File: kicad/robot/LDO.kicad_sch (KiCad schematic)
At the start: 20 parts, among them U14 MAX77642ANA+

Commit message: Exported all schematic symbols to local robot and refer to them in all symbols
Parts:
- C4, C84, C85, C87, C88, C92, C93: symbol Device:C -> robot:C
- JP22: symbol Jumper:Jumper -> robot:Jumper
- JP7: symbol Jumper:Jumper_2_Bridged -> robot:Jumper_2_Bridged
- L3: symbol Device:L -> robot:L
- R53, R55, R9: symbol Device:R -> robot:R
- U14: symbol Regulator_Switching:MAX77642ANA+ -> robot:MAX77642ANA+
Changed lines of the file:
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@@
     (effects (font (size 1.27 1.27)) (justify right))
   )
-  (symbol (lib_id "Device:R") (at 26.67 106.68 0) (unit 1)
+  (symbol (lib_id "robot:R") (at 26.67 106.68 0) (unit 1)
     (in_bom yes) (on_board yes) (dnp no)
     (property "Reference" "R53" (at 29.21 105.4099 0)
@@
     )
   )
-  (symbol (lib_id "Device:C") (at 196.85 86.36 0) (mirror y) (unit 1)
+  (symbol (lib_id "robot:C") (at 196.85 86.36 0) (mirror y) (unit 1)
     (in_bom yes) (on_board yes) (dnp no)
     (property "Reference" "C93" (at 193.04 83.8199 0)
@@
     )
   )
-  (symbol (lib_id "Device:C") (at 151.13 88.9 0) (mirror y) (unit 1)
+  (symbol (lib_id "robot:C") (at 151.13 88.9 0) (mirror y) (unit 1)
     (in_bom yes) (on_board yes) (dnp no)
     (property "Reference" "C88" (at 147.32 86.3599 0)
@@
     )
   )
-  (symbol (lib_id "Jumper:Jumper_2_Bridged") (at 213.36 77.47 0) (unit 1)
+  (symbol (lib_id "robot:Jumper_2_Bridged") (at 213.36 77.47 0) (unit 1)
     (in_bom yes) (on_board yes) (dnp no)
     (property "Reference" "JP7" (at 213.36 74.93 0)
@@
     )
   )
-  (symbol (lib_id "Device:R") (at 46.99 106.68 0) (unit 1)
+  (symbol (lib_id "robot:R") (at 46.99 106.68 0) (unit 1)
     (in_bom yes) (on_board yes) (dnp no)
     (property "Reference" "R9" (at 49.53 105.4099 0)
@@
     )
   )
-  (symbol (lib_id "Device:C") (at 149.86 68.58 0) (mirror y) (unit 1)
+  (symbol (lib_id "robot:C") (at 149.86 68.58 0) (mirror y) (unit 1)
     (in_bom yes) (on_board yes) (dnp no)
     (property "Reference" "C87" (at 146.05 66.0399 0)
@@
     )
   )
-  (symbol (lib_id "Jumper:Jumper_2_Bridged") (at 127 100.33 0) (unit 1)
+  (symbol (lib_id "robot:Jumper_2_Bridged") (at 127 100.33 0) (unit 1)
     (in_bom yes) (on_board yes) (dnp no)
     (property "Reference" "JP7" (at 127 97.79 0)
@@
     )
   )
-  (symbol (lib_id "Jumper:Jumper") (at 158.75 85.09 0) (unit 1)
+  (symbol (lib_id "robot:Jumper") (at 158.75 85.09 0) (unit 1)
     (in_bom yes) (on_board yes) (dnp no)
     (property "Reference" "JP22" (at 158.75 86.36 0)
@@
     )
   )
-  (symbol (lib_id "Device:L") (at 62.23 72.39 90) (unit 1)
+  (symbol (lib_id "robot:L") (at 62.23 72.39 90) (unit 1)
     (in_bom yes) (on_board yes) (dnp no) (fields_autoplaced)
     (property "Reference" "L3" (at 62.23 66.04 90)
@@
     )
   )
-  (symbol (lib_id "Jumper:Jumper_2_Bridged") (at 158.75 85.09 0) (unit 1)
+  (symbol (lib_id "robot:Jumper_2_Bridged") (at 158.75 85.09 0) (unit 1)
     (in_bom yes) (on_board yes) (dnp no)
     (property "Reference" "JP7" (at 158.75 82.55 0)
@@
     )
   )
-  (symbol (lib_id "Jumper:Jumper") (at 127 92.71 0) (unit 1)
+  (symbol (lib_id "robot:Jumper") (at 127 92.71 0) (unit 1)
     (in_bom yes) (on_board yes) (dnp no)
     (property "Reference" "JP22" (at 127 93.98 0)
@@
     )
   )
-  (symbol (lib_id "Jumper:Jumper") (at 127 100.33 0) (unit 1)
+  (symbol (lib_id "robot:Jumper") (at 127 100.33 0) (unit 1)
     (in_bom yes) (on_board yes) (dnp no)
     (property "Reference" "JP22" (at 127 101.6 0)
@@
     )
   )
-  (symbol (lib_id "Regulator_Switching:MAX77642ANA+") (at 69.85 64.77 0) (unit 1)
+  (symbol (lib_id "robot:MAX77642ANA+") (at 69.85 64.77 0) (unit 1)
     (in_bom yes) (on_board yes) (dnp no) (fields_autoplaced)
     (property "Reference" "U14" (at 92.71 57.15 0)
@@
     )
   )
-  (symbol (lib_id "Jumper:Jumper") (at 213.36 77.47 0) (unit 1)
+  (symbol (lib_id "robot:Jumper") (at 213.36 77.47 0) (unit 1)
     (in_bom yes) (on_board yes) (dnp no)
     (property "Reference" "JP22" (at 213.36 78.74 0)
@@
     )
   )
-  (symbol (lib_id "Device:C") (at 134.62 68.58 0) (mirror y) (unit 1)
+  (symbol (lib_id "robot:C") (at 134.62 68.58 0) (mirror y) (unit 1)
     (in_bom yes) (on_board yes) (dnp no)
     (property "Reference" "C85" (at 130.81 66.0399 0)
@@
     )
   )
-  (symbol (lib_id "Jumper:Jumper_2_Bridged") (at 127 92.71 0) (unit 1)
+  (symbol (lib_id "robot:Jumper_2_Bridged") (at 127 92.71 0) (unit 1)
     (in_bom yes) (on_board yes) (dnp no)
     (property "Reference" "JP7" (at 127 90.17 0)
@@
     )
   )
-  (symbol (lib_id "Device:C") (at 43.18 68.58 0) (mirror y) (unit 1)
+  (symbol (lib_id "robot:C") (at 43.18 68.58 0) (mirror y) (unit 1)
     (in_bom yes) (on_board yes) (dnp no)
     (property "Reference" "C4" (at 39.37 66.0399 0)
@@
     )
   )
-  (symbol (lib_id "Device:C") (at 184.15 86.36 0) (mirror y) (unit 1)
+  (symbol (lib_id "robot:C") (at 184.15 86.36 0) (mirror y) (unit 1)
     (in_bom yes) (on_board yes) (dnp no)
     (property "Reference" "C92" (at 180.34 83.8199 0)
@@
     )
   )
-  (symbol (lib_id "Device:R") (at 64.77 106.68 0) (unit 1)
+  (symbol (lib_id "robot:R") (at 64.77 106.68 0) (unit 1)
     (in_bom yes) (on_board yes) (dnp no)
     (property "Reference" "R55" (at 67.31 105.4099 0)
@@
     )
   )
-  (symbol (lib_id "Device:C") (at 61.595 82.55 90) (mirror x) (unit 1)
+  (symbol (lib_id "robot:C") (at 61.595 82.55 90) (mirror x) (unit 1)
     (in_bom yes) (on_board yes) (dnp no)
     (property "Reference" "C84" (at 62.865 86.36 90)

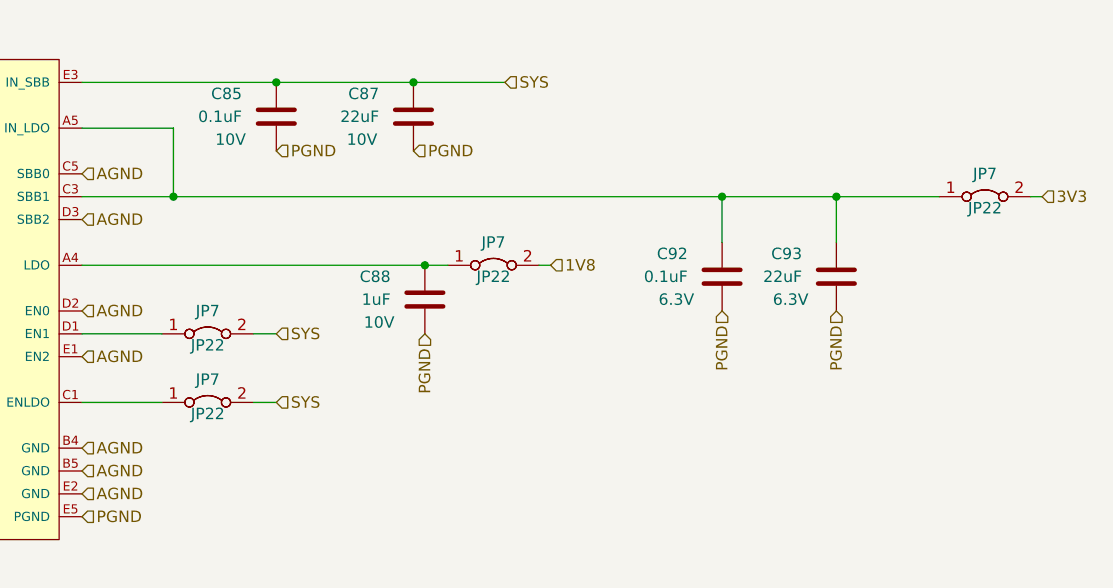
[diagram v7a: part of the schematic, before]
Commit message: Replaced all jumpers with 0 ohm resistors
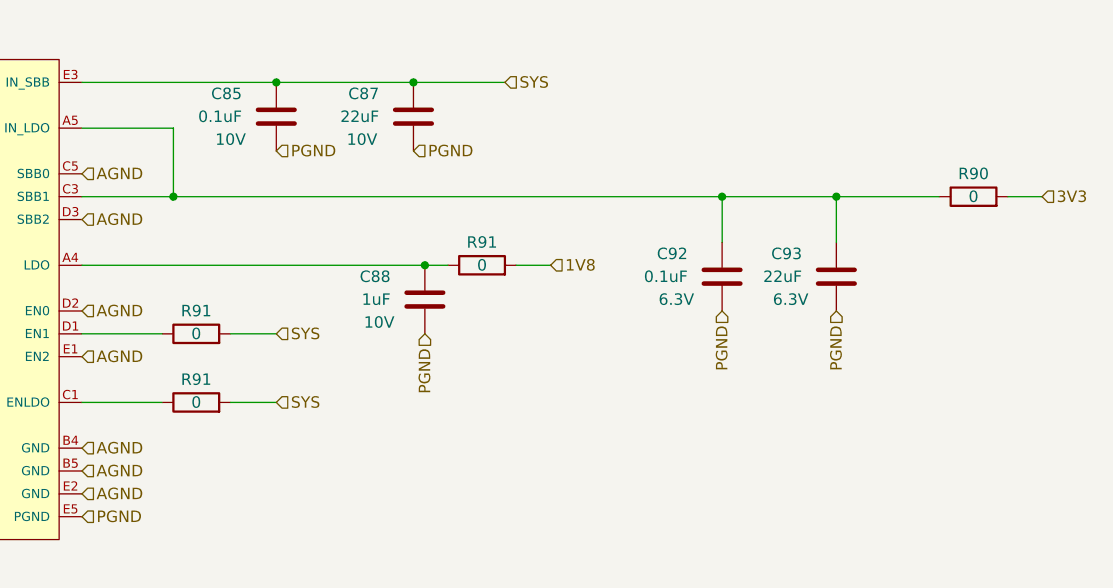
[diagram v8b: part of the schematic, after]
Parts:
- removed JP22 (x4): Jumper, robot:2.54mm_2pointJumper, symbol robot:Jumper
- removed JP7 (x4): Jumper_Bridged, robot:2.54mm_2pointJumperClosed, symbol robot:Jumper_2_Bridged
- added R90, R91 (x3): 0, robot:R_0603_1608Metric, symbol Device:R
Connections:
- net 1V8: now also R91.2
- net 3V3: now also R90.2
- net SYS: now also R91.2, R91.2
- net at C92.1, C93.1, U14.A5 (IN_LDO)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: now also R90.1
- net at C88.1, U14.A4 (LDO): now also R91.1
- net at U14.C1 (ENLDO): now also R91.1
- net at U14.D1 (EN1): now also R91.1
